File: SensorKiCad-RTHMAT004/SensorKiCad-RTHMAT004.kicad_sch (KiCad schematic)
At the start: 13 parts, among them J1 Conn_02x14_Odd_Even_MountingP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, Q1 2N2219, Q2 2N2219

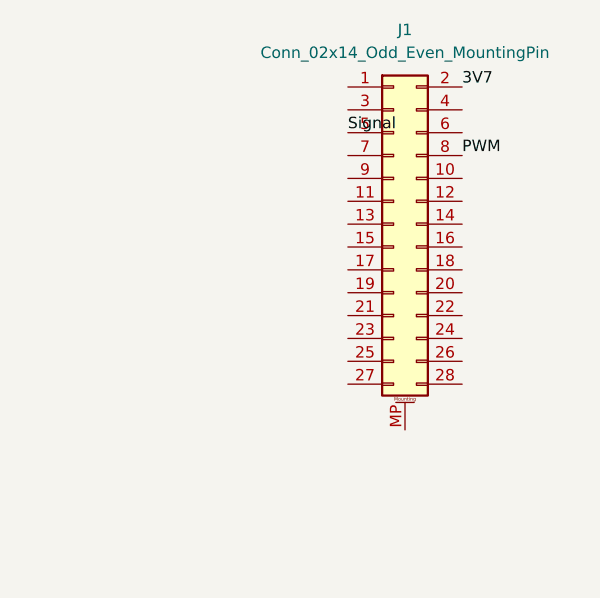
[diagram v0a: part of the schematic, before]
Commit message: Unpopulated pins
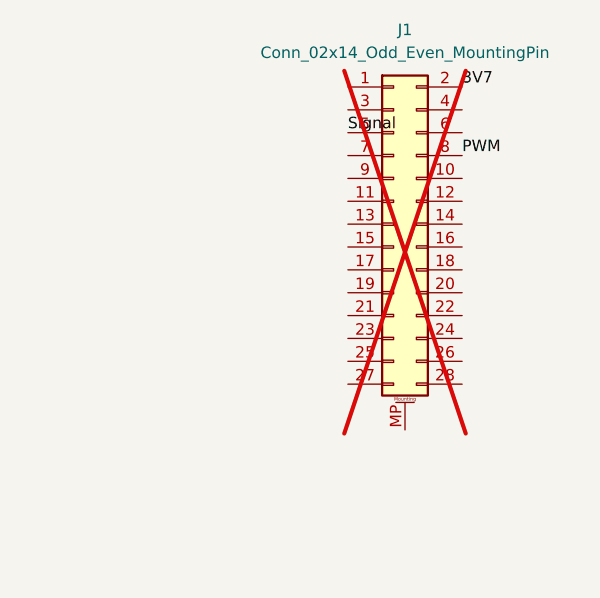
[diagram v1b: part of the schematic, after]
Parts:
- J1: now not fitted
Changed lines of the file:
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@@
 		(in_bom yes)
 		(on_board yes)
-		(dnp no)
+		(dnp yes)
 		(fields_autoplaced yes)
 		(property "Reference" "J1"

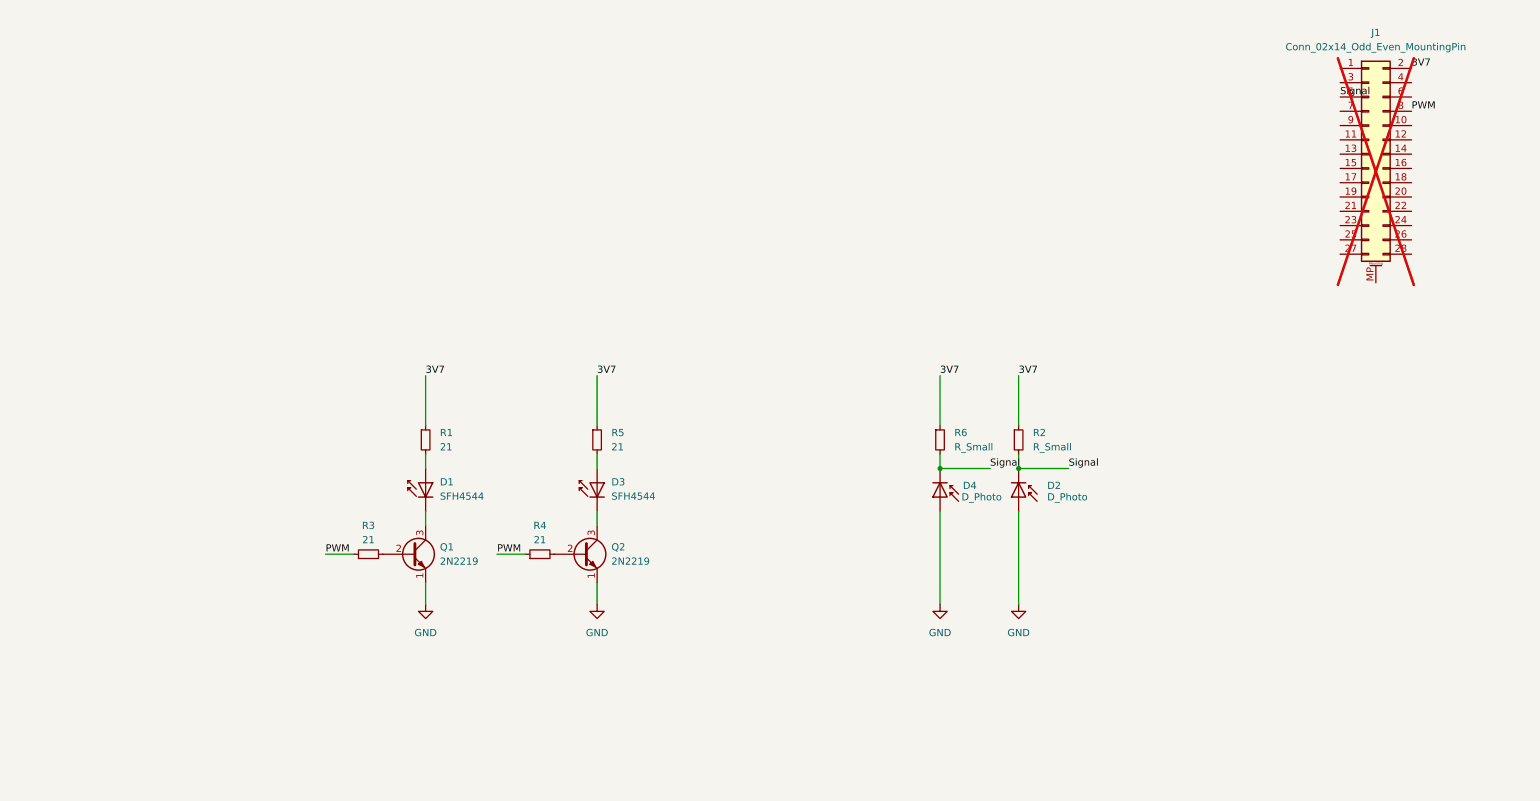
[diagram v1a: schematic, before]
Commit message: Small changes to Sensor KiCAD file
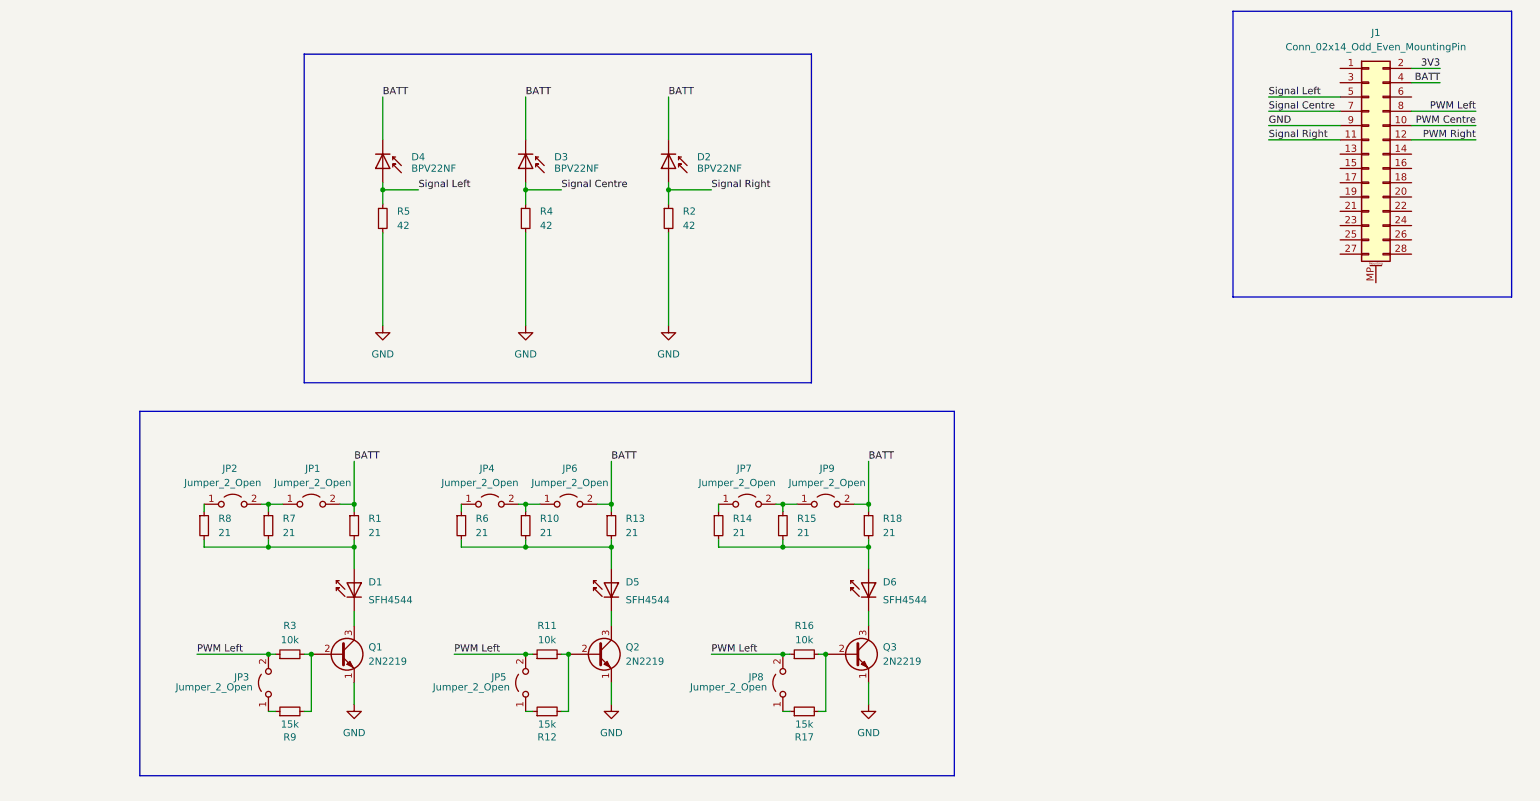
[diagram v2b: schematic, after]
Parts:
- removed D3: SFH4544, symbol LED:SFH4546
- added D3: BPV22NF, symbol Device:D_Photo
- added D5, D6: SFH4544, symbol LED:SFH4546
- added JP1, JP2, JP3, JP4, JP5, JP6, JP7, JP8, JP9: Jumper_2_Open, symbol Jumper:Jumper_2_Open
- added Q3: 2N2219, Package_TO_SOT_THT:TO-39-3, symbol Transistor_BJT:2N2219
- added R10, R13, R14, R15, R18, R7, R8: 21, symbol Device:R_Small
- added R11, R16: 10k, symbol Device:R_Small
- added R12, R17, R9: 15k, symbol Device:R_Small
- D2, D4: value D_Photo -> BPV22NF; Extended (none) -> 1; LCSC (none) -> C130226; Populate (none) -> 1; Price (none) -> 0.48
- J1: now fitted
- R2: value R_Small -> 42
- R3: value 21 -> 10k
- R4: value 21 -> 42
- R5: value 21 -> 42; footprint (none) -> Resistor_SMD:R_0805_2012Metric
- R6: value R_Small -> 21
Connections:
- net GND: now also J1.9 (Pin_9), R2.2, R4.2, R5.2, Q3.1 (E); no longer D2.2 (A), D4.2 (A)
- net at Q1.2 (B), R3.2: now also R9.2
- net at D1.2 (A), R1.2: now also R7.2, R8.2
- net at Q2.2 (B): now also R11.2, R12.2; no longer R4.2
- net at Q2.3 (C): now also D5.1 (K)
- net PWM Centre: now reaches J1.10 (Pin_10)
- net Signal Right: now reaches J1.11 (Pin_11)
- net Signal Right: now also D2.2 (A), R2.1
- net PWM Right: now reaches J1.12 (Pin_12)
- net BATT: now reaches J1.4 (Pin_4)
- net BATT: now also D2.1 (K), D4.1 (K), R1.1, D3.1 (K), JP1.2 (B), JP6.2 (B), JP9.2 (B), R13.1, R18.1
- net Signal Centre: now reaches J1.7 (Pin_7)
- net Signal Centre: now also R4.1, D3.2 (A)
- removed net 3V7: J1.2 (Pin_2), R1.1, R2.1, R5.1, R6.1
- net PWM renamed PWM Left
- net PWM Left: now also JP3.2 (B), JP5.2 (B), JP8.2 (B), R11.1, R16.1; no longer R4.1
- removed net Signal: D2.1 (K), D4.1 (K), J1.5 (Pin_5), R2.2, R6.2
- new net: JP3.1 (A), R9.1
- new net: Q3.2 (B), R16.2, R17.2
- new net: D6.1 (K), Q3.3 (C)
- new net: D6.2 (A), R14.2, R15.2, R18.2
- new net: JP2.1 (A), R8.1
- new net: JP1.1 (A), JP2.2 (B), R7.1
- new net: JP8.1 (A), R17.1
- new net: D5.2 (A), R10.2, R13.2, R6.2
- new net: JP7.2 (B), JP9.1 (A), R15.1
- new net: JP7.1 (A), R14.1
- new net: JP4.2 (B), JP6.1 (A), R10.1
- new net: JP4.1 (A), R6.1
- new net: JP5.1 (A), R12.1
- new net 3V3: J1.2 (Pin_2)
- new net Signal Left: D4.2 (A), J1.5 (Pin_5), R5.1
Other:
- moved on the sheet: D1, D2, Q1, R1, R2, R3

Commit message: Small changes to Sensor KiCAD file
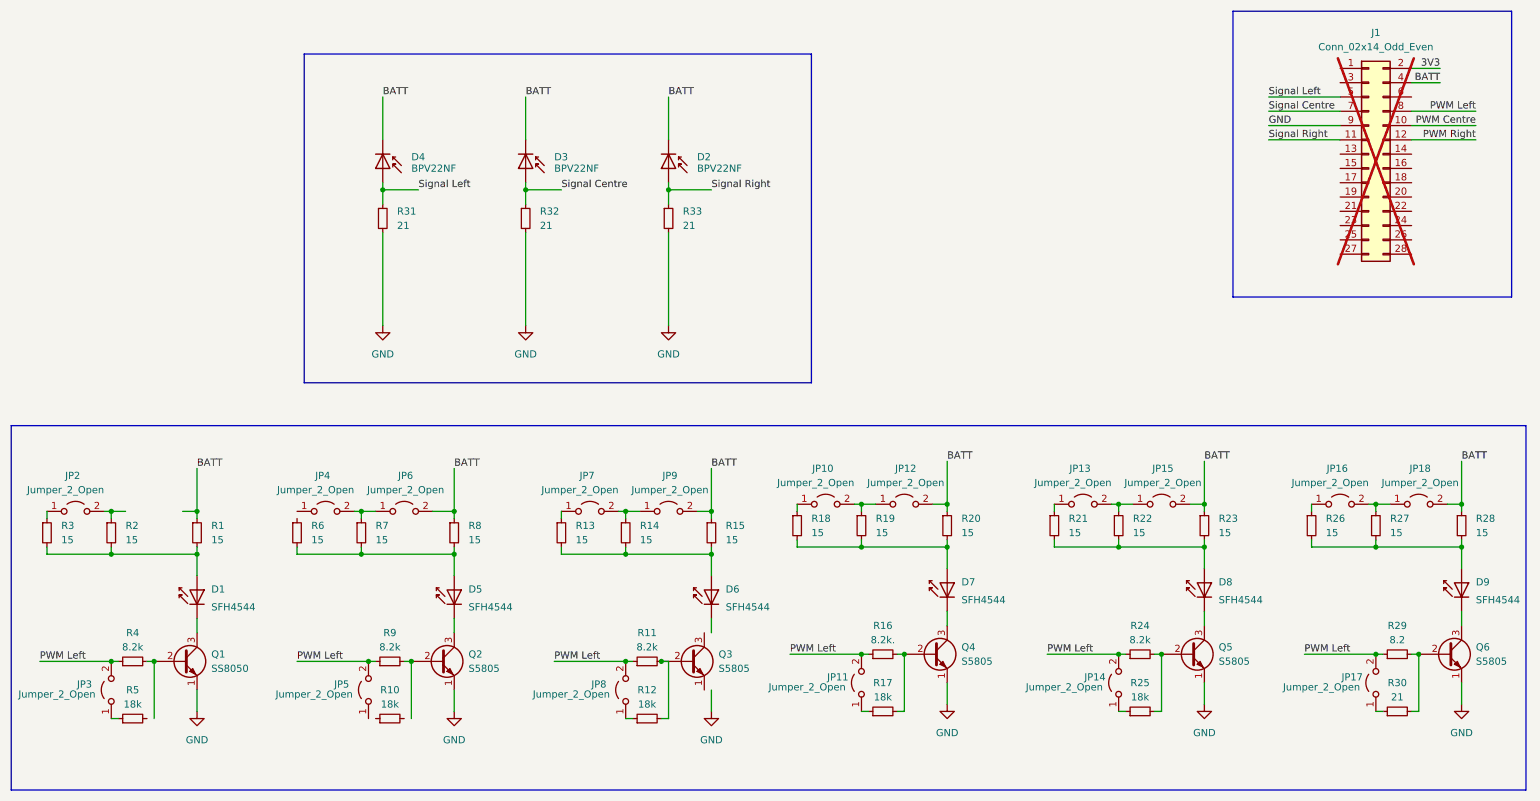
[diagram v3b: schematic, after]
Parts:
- removed J1: Conn_02x14_Odd_Even_MountingPin, symbol Connector_Generic_MountingPin:Conn_02x14_Odd_Even_MountingPin
- removed JP1: Jumper_2_Open, symbol Jumper:Jumper_2_Open
- added D7, D8, D9: SFH4544, LED_THT:LED_D3.0mm_IRBlack, symbol LED:SFH4546
- added J1: Conn_02x14_Odd_Even, Connector_PinHeader_1.00mm:PinHeader_2x14_P1.00mm_Vertical, symbol Connector_Generic:Conn_02x14_Odd_Even
- added JP10, JP11, JP12, JP13, JP14, JP15, JP16, JP17, JP18: Jumper_2_Open, Jumper:SolderJumper-2_P1.3mm_Open_RoundedPad1.0x1.5mm, symbol Jumper:Jumper_2_Open
- added Q4, Q5, Q6: S5805, Package_TO_SOT_THT:TO-39-3, symbol Transistor_BJT:2N2219
- added R19, R20, R21, R22, R23, R26, R27, R28: 15, Resistor_SMD:R_0815_2038Metric, symbol Device:R_Small
- added R24: 8.2k, Resistor_SMD:R_0815_2038Metric, symbol Device:R_Small
- added R25: 18k, Resistor_SMD:R_0815_2038Metric, symbol Device:R_Small
- added R29: 8.2, Resistor_SMD:R_0815_2038Metric, symbol Device:R_Small
- added R30, R31, R32, R33: 21, Resistor_SMD:R_0815_2038Metric, symbol Device:R_Small
- D1, D5, D6: footprint (none) -> LED_THT:LED_D3.0mm_IRBlack
- D2, D3, D4: footprint (none) -> LED_THT:LED_D3.0mm_IRBlack; LCSC C130226 -> C2900370
- JP2, JP3, JP4, JP5, JP6, JP7, JP8, JP9: footprint (none) -> Jumper:SolderJumper-2_P1.3mm_Open_RoundedPad1.0x1.5mm
- Q1: value 2N2219 -> SS8050; footprint Package_TO_SOT_THT:TO-39-3 -> Package_TO_SOT_SMD:SOT-23; LCSC (none) -> C2150
- Q2, Q3: value 2N2219 -> S5805; LCSC (none) -> C2150
- R1, R13, R14, R15, R18, R6, R7, R8: value 21 -> 15; footprint (none) -> Resistor_SMD:R_0815_2038Metric
- R10: value 21 -> 18k; footprint (none) -> Resistor_SMD:R_0815_2038Metric
- R11: value 10k -> 8.2k; footprint (none) -> Resistor_SMD:R_0815_2038Metric
- R12, R17: value 15k -> 18k; footprint (none) -> Resistor_SMD:R_0815_2038Metric
- R16: value 10k -> 8.2k.; footprint (none) -> Resistor_SMD:R_0815_2038Metric
- R2: value 42 -> 15; footprint (none) -> Resistor_SMD:R_0815_2038Metric
- R3: value 10k -> 15; footprint (none) -> Resistor_SMD:R_0815_2038Metric
- R4: value 42 -> 8.2k; footprint (none) -> Resistor_SMD:R_0815_2038Metric
- R5: value 42 -> 18k; footprint Resistor_SMD:R_0805_2012Metric -> Resistor_SMD:R_0815_2038Metric
- R9: value 15k -> 8.2k; footprint (none) -> Resistor_SMD:R_0815_2038Metric
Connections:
- net 3V3: now also J1.2 (Pin_2)
- net BATT: now also R15.1, R8.1, J1.4 (Pin_4), JP12.2 (B), JP15.2 (B), JP18.2 (B), R20.1, R23.1, R28.1; no longer R13.1, R18.1
- net GND: now also J1.9 (Pin_9), Q4.1 (E), Q5.1 (E), Q6.1 (E), R31.2, R32.2, R33.2; no longer Q3.1 (E), R2.2, R4.2, R5.2
- net PWM Centre: now also J1.10 (Pin_10)
- net PWM Left: now also R4.1, R9.1, J1.8 (Pin_8), JP11.2 (B), JP14.2 (B), JP17.2 (B), R24.1, R29.1; no longer R3.1
- net PWM Right: now also J1.12 (Pin_12)
- net Signal Centre: now also J1.7 (Pin_7), R32.1; no longer R4.1
- net Signal Left: now also J1.5 (Pin_5), R31.1; no longer R5.1
- net Signal Right: now also J1.11 (Pin_11), R33.1; no longer R2.1
- net at JP3.1 (A): now also R5.1; no longer R9.1
- net at R16.2, R17.2: now also Q4.2 (B); no longer Q3.2 (B)
- net at D6.1 (K): no longer Q3.3 (C)
- net at D6.2 (A), R14.2, R15.2: now also R13.2; no longer R18.2
- net at JP2.1 (A): now also R3.1; no longer R8.1
- net at JP2.2 (B): now also R2.1; no longer R7.1
- net at R17.1: now also JP11.1 (A); no longer JP8.1 (A)
- net at D5.2 (A), R6.2: now also R7.2, R8.2; no longer R10.2, R13.2
- net at JP7.2 (B), JP9.1 (A): now also R14.1; no longer R15.1
- net at D1.2 (A), R1.2: now also R2.2, R3.2; no longer R7.2, R8.2
- net at JP7.1 (A): now also R13.1; no longer R14.1
- net at R11.2, R12.2: now also Q3.2 (B); no longer Q2.2 (B)
- net at JP4.2 (B), JP6.1 (A): now also R7.1; no longer R10.1
- net at R6.1: no longer JP4.1 (A)
- net at R12.1: now also JP8.1 (A); no longer JP5.1 (A)
- new net: Q1.2 (B), R4.2
- new net: D7.1 (K), Q4.3 (C)
- new net: Q2.2 (B), R9.2
- new net: D7.2 (A), R18.2, R19.2, R20.2
- new net: JP14.1 (A), R25.1
- new net: Q5.2 (B), R24.2, R25.2
- new net: Q6.2 (B), R29.2, R30.2
- new net: D8.2 (A), R21.2, R22.2, R23.2
- new net: JP17.1 (A), R30.1
- new net: JP13.2 (B), JP15.1 (A), R22.1
- new net: JP10.1 (A), R18.1
- new net: D8.1 (K), Q5.3 (C)
- new net: JP13.1 (A), R21.1
- new net: JP10.2 (B), JP12.1 (A), R19.1
- new net: JP16.2 (B), JP18.1 (A), R27.1
- new net: JP16.1 (A), R26.1
- new net: D9.1 (K), Q6.3 (C)
- new net: D9.2 (A), R26.2, R27.2, R28.2
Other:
- moved on the sheet: D1, D5, D6, JP2, JP3, JP4, JP5, JP6, JP7, JP8, JP9, Q1

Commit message: Small changes to Sensor KiCAD file
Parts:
- added JP1: Jumper_2_Open, Jumper:SolderJumper-2_P1.3mm_Open_RoundedPad1.0x1.5mm, symbol Jumper:Jumper_2_Open
- D2, D3, D4: footprint LED_THT:LED_D3.0mm_IRBlack -> LED_THT:LED_SideEmitter_Rectangular_W4.5mm_H1.6mm
- J1: footprint Connector_PinHeader_1.00mm:PinHeader_2x14_P1.00mm_Vertical -> Connector_PinHeader_2.54mm:PinHeader_2x14_P2.54mm_Vertical
- Q2, Q3, Q4, Q5, Q6: value S5805 -> SS8050; footprint Package_TO_SOT_THT:TO-39-3 -> Package_TO_SOT_SMD:SOT-23
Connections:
- net BATT: now also JP1.2 (B)
- net GND: now also Q3.1 (E)
- net PWM Centre: now also JP11.2 (B), JP8.2 (B), R11.1, R16.1
- net PWM Left: no longer JP11.2 (B), JP14.2 (B), JP17.2 (B), JP8.2 (B), R11.1, R16.1, R24.1, R29.1
- net PWM Right: now also JP14.2 (B), JP17.2 (B), R24.1, R29.1
- net at Q1.2 (B), R4.2: now also R5.2
- net at Q2.2 (B), R9.2: now also R10.2
- net at D6.1 (K): now also Q3.3 (C)
- net at JP2.2 (B), R2.1: now also JP1.1 (A)
- net at R6.1: now also JP4.1 (A)
- net at R10.1: now also JP5.1 (A)
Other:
- moved on the sheet: Q3
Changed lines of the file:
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@@
 	)
 	(junction
+		(at 130.81 132.08)
+		(diameter 0)
+		(color 0 0 0 0)
+	)
+	(junction
 		(at 172.72 130.81)
 		(diameter 0)
@@
 	)
 	(junction
-		(at 129.54 132.08)
-		(diameter 0)
-		(color 0 0 0 0)
-	)
-	(junction
 		(at 123.19 105.41)
 		(diameter 0)
@@
 	(wire
 		(pts
+			(xy 64.77 105.41) (xy 64.77 106.68)
+		)
+		(stroke
+			(width 0)
+			(type default)
+		)
+	)
+	(wire
+		(pts
 			(xy 237.49 31.75) (xy 250.19 31.75)
 		)
@@
 	(wire
 		(pts
+			(xy 38.1 142.24) (xy 39.37 142.24)
+		)
+		(stroke
+			(width 0)
+			(type default)
+		)
+	)
+	(wire
+		(pts
 			(xy 111.76 105.41) (xy 111.76 106.68)
 		)
@@
 	(wire
 		(pts
+			(xy 77.47 142.24) (xy 78.74 142.24)
+		)
+		(stroke
+			(width 0)
+			(type default)
+		)
+	)
+	(wire
+		(pts
 			(xy 19.05 132.08) (xy 31.75 132.08)
 		)
@@
 	(wire
 		(pts
+			(xy 83.82 142.24) (xy 85.09 142.24)
+		)
+		(stroke
+			(width 0)
+			(type default)
+		)
+	)
+	(wire
+		(pts
 			(xy 271.78 104.14) (xy 271.78 105.41)
 		)
@@
 		)
 	)
-	(label "PWM Left"
+	(label "PWM Right"
 		(at 198.12 130.81 0)
 		(fields_autoplaced yes)
@@
 		)
 	)
-	(label "PWM Left"
+	(label "PWM Centre"
 		(at 110.49 132.08 0)
 		(fields_autoplaced yes)
@@
 		)
 	)
-	(label "PWM Left"
+	(label "PWM Centre"
 		(at 152.4 130.81 0)
 		(fields_autoplaced yes)
@@
 		)
 	)
-	(label "PWM Left"
+	(label "PWM Right"
 		(at 243.84 130.81 0)
 		(fields_autoplaced yes)
@@
 			)
 		)
-		(property "Value" "S5805"
+		(property "Value" "SS8050"
 			(at 182.88 132.0799 0)
 			(effects
@@
 			)
 		)
-		(property "Footprint" "Package_TO_SOT_THT:TO-39-3"
+		(property "Footprint" "Package_TO_SOT_SMD:SOT-23"
 			(at 182.88 132.715 0)
 			(effects
@@
 	(symbol
 		(lib_id "Transistor_BJT:2N2219")
-		(at 134.62 132.08 0)
+		(at 135.89 132.08 0)
 		(unit 1)
 		(exclude_from_sim no)
@@
 		(fields_autoplaced yes)
 		(property "Reference" "Q3"
-			(at 139.7 130.8099 0)
+			(at 140.97 130.8099 0)
 			(effects
 				(font
@@
 			)
 		)
-		(property "Value" "S5805"
-			(at 139.7 133.3499 0)
+		(property "Value" "SS8050"
+			(at 140.97 133.3499 0)
 			(effects
 				(font
@@
 			)
 		)
-		(property "Footprint" "Package_TO_SOT_THT:TO-39-3"
-			(at 139.7 133.985 0)
+		(property "Footprint" "Package_TO_SOT_SMD:SOT-23"
+			(at 140.97 133.985 0)
 			(effects
 				(font
@@
 		)
 		(property "Datasheet" "http://www.onsemi.com/pub_link/Collateral/2N2219-D.PDF"
-			(at 134.62 132.08 0)
+			(at 135.89 132.08 0)
 			(effects
 				(font
@@
 		)
 		(property "Description" "800mA Ic, 50V Vce, NPN Transistor, TO-39"
-			(at 134.62 132.08 0)
+			(at 135.89 132.08 0)
 			(effects
 				(font
@@
 		)
 		(property "LCSC" "C2150"
-			(at 134.62 132.08 0)
+			(at 135.89 132.08 0)
 			(effects
 				(font
@@
 			)
 		)
-		(property "Footprint" "LED_THT:LED_D3.0mm_IRBlack"
+		(property "Footprint" "LED_THT:LED_SideEmitter_Rectangular_W4.5mm_H1.6mm"
 			(at 80.01 43.18 0)
 			(effects
@@
 			)
 		)
-		(property "Footprint" "LED_THT:LED_D3.0mm_IRBlack"
+		(property "Footprint" "LED_THT:LED_SideEmitter_Rectangular_W4.5mm_H1.6mm"
 			(at 130.81 43.18 0)
 			(effects
@@
 			)
 		)
-		(property "Value" "S5805"
+		(property "Value" "SS8050"
 			(at 228.6 132.0799 0)
 			(effects
@@
 			)
 		)
-		(property "Footprint" "Package_TO_SOT_THT:TO-39-3"
+		(property "Footprint" "Package_TO_SOT_SMD:SOT-23"
 			(at 228.6 132.715 0)
 			(effects
@@
 			)
 		)
-		(property "Footprint" "LED_THT:LED_D3.0mm_IRBlack"
+		(property "Footprint" "LED_THT:LED_SideEmitter_Rectangular_W4.5mm_H1.6mm"
 			(at 105.41 43.18 0)
 			(effects
@@
 			)
 		)
-		(property "Footprint" "Connector_PinHeader_1.00mm:PinHeader_2x14_P1.00mm_Vertical"
+		(property "Footprint" "Connector_PinHeader_2.54mm:PinHeader_2x14_P2.54mm_Vertical"
 			(at 255.27 41.91 0)
 			(effects
@@
 			)
 		)
-		(property "Value" "S5805"
+		(property "Value" "SS8050"
 			(at 95.25 133.3499 0)
 			(effects
@@
 			)
 		)
-		(property "Footprint" "Package_TO_SOT_THT:TO-39-3"
+		(property "Footprint" "Package_TO_SOT_SMD:SOT-23"
 			(at 95.25 133.985 0)
 			(effects
@@
 	(symbol
 		(lib_id "Jumper:Jumper_2_Open")
+		(at 39.37 105.41 0)
+		(unit 1)
+		(exclude_from_sim no)
+		(in_bom yes)
+		(on_board yes)
+		(dnp no)
+		(fields_autoplaced yes)
+		(property "Reference" "JP1"
+			(at 39.37 99.06 0)
+			(effects
+				(font
+					(size 1.27 1.27)
+				)
+			)
+		)
+		(property "Value" "Jumper_2_Open"
+			(at 39.37 101.6 0)
+			(effects
+				(font
+					(size 1.27 1.27)
+				)
+			)
+		)
+		(property "Footprint" "Jumper:SolderJumper-2_P1.3mm_Open_RoundedPad1.0x1.5mm"
+			(at 39.37 105.41 0)
+			(effects
+				(font
+					(size 1.27 1.27)
+				)
+				(hide yes)
+			)
+		)
+		(property "Datasheet" "~"
+			(at 39.37 105.41 0)
+			(effects
+				(font
+					(size 1.27 1.27)
+				)
+				(hide yes)
+			)
+		)
+		(property "Description" "Jumper, 2-pole, open"
+			(at 39.37 105.41 0)
+			(effects
+				(font
+					(size 1.27 1.27)
+				)
+				(hide yes)
+			)
+		)
+		(pin "2"
+		)
+		(pin "1"
+		)
+		(instances
+			(project "SensorKiCad-RTHMAT004"
+				(path "/c05e1c56-18bc-4f90-8ce8-a924fef2dce9"
+					(reference "JP1")
+					(unit 1)
+				)
+			)
+		)
+	)
+	(symbol
+		(lib_id "Jumper:Jumper_2_Open")
 		(at 158.75 104.14 0)
 		(unit 1)
@@
 			)
 		)
-		(property "Value" "S5805"
+		(property "Value" "SS8050"
 			(at 274.32 132.0799 0)
 			(effects
@@
 			)
 		)
-		(property "Footprint" "Package_TO_SOT_THT:TO-39-3"
+		(property "Footprint" "Package_TO_SOT_SMD:SOT-23"
 			(at 274.32 132.715 0)
 			(effects
